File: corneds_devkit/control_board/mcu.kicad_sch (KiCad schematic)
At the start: 1 part, among them U1 nRF52832-QFxx

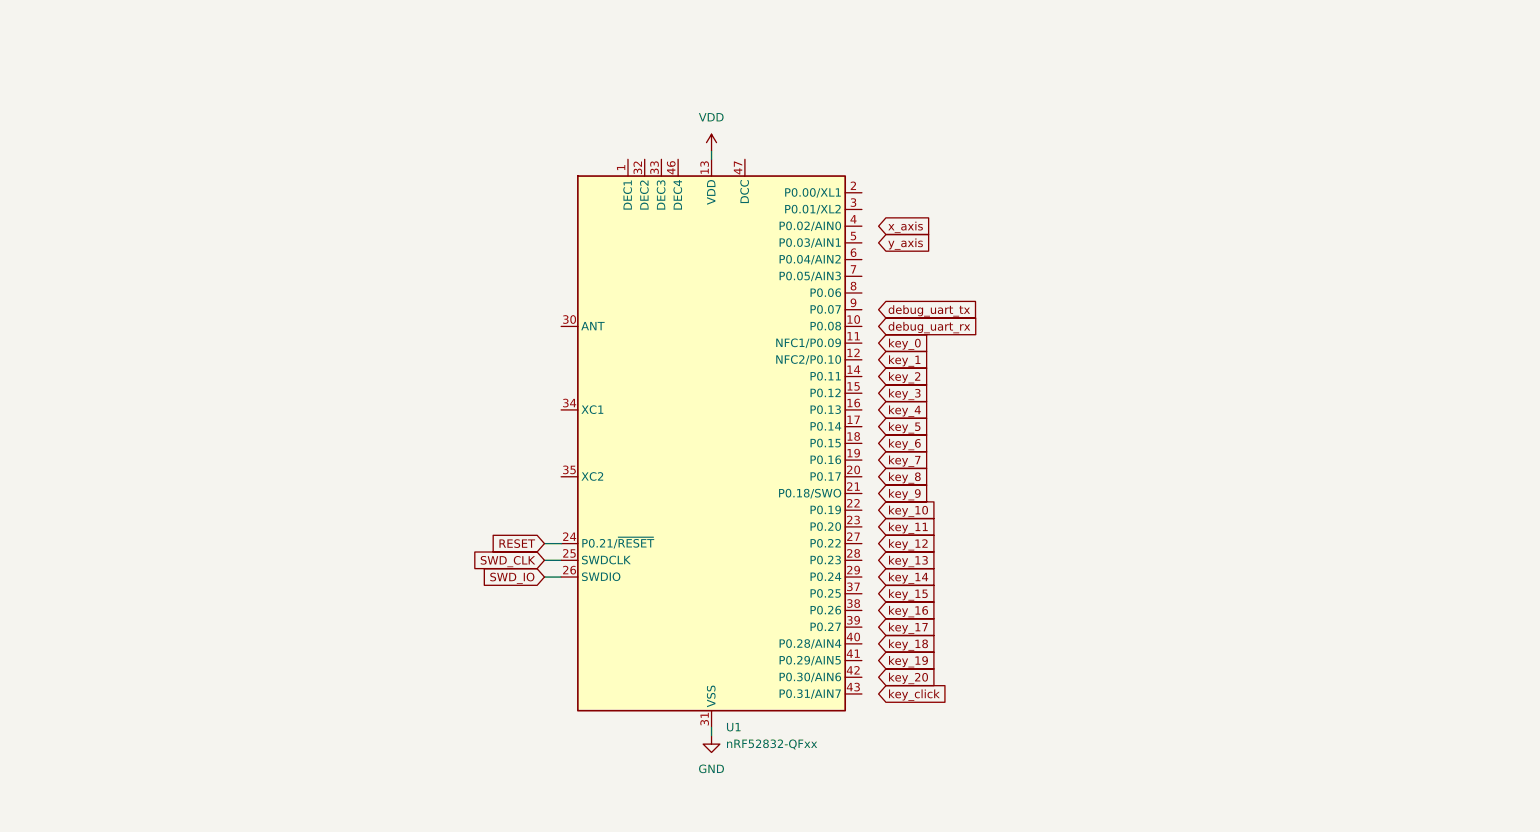
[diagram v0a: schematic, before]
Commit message: finished routing power board and started on control board schematic but realized I need seperate reset lines
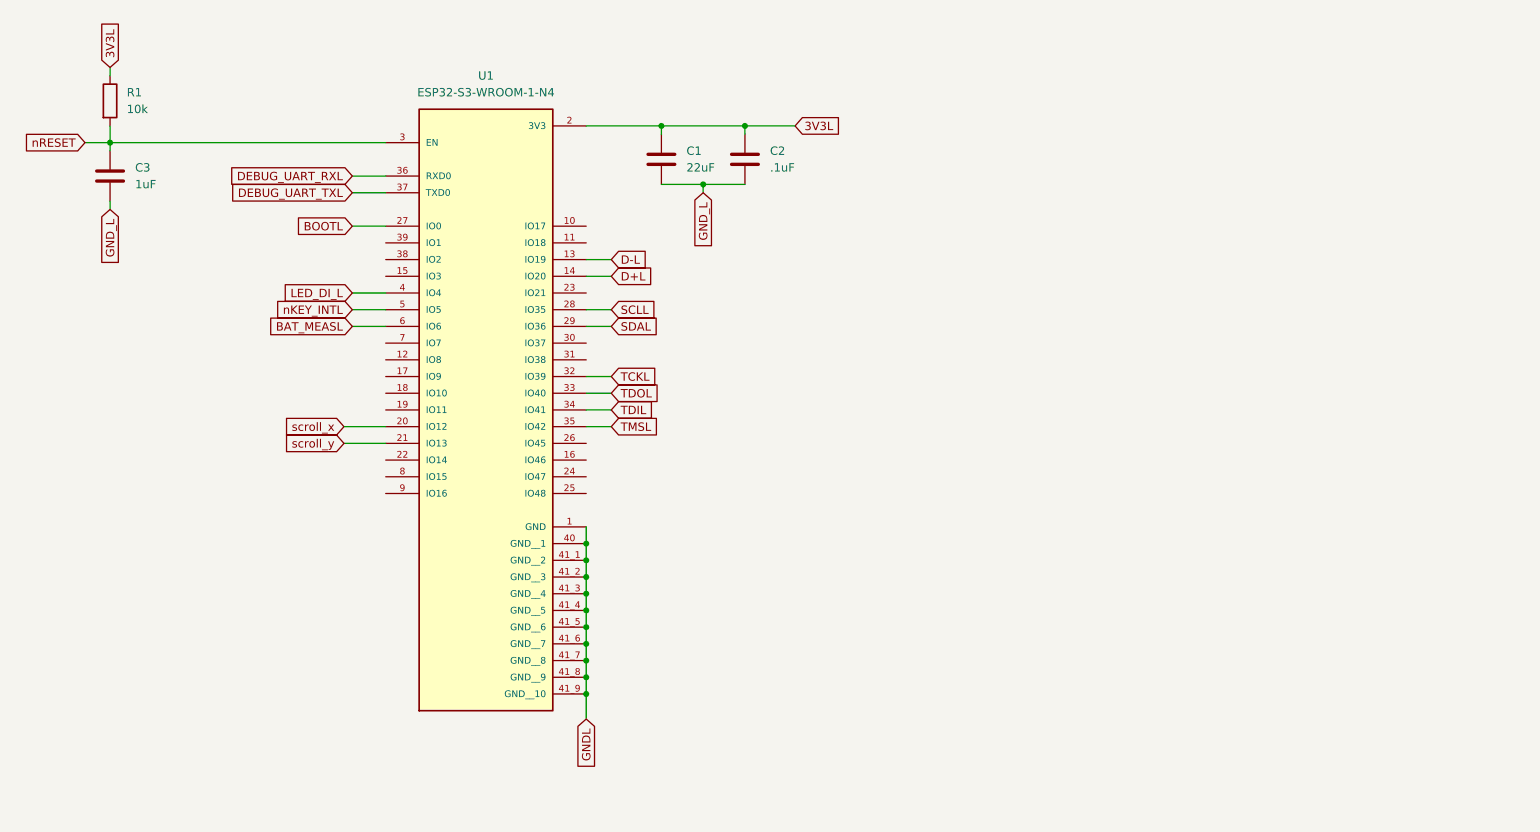
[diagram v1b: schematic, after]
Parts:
- removed U1: nRF52832-QFxx, Package_DFN_QFN:QFN-48-1EP_6x6mm_P0.4mm_EP4.6x4.6mm, symbol MCU_Nordic:nRF52832-QFxx
- added C1: 22uF, Capacitor_SMD:C_0402_1005Metric, symbol Device:C
- added C2: .1uF, Capacitor_SMD:C_0402_1005Metric, symbol Device:C
- added C3: 1uF, Capacitor_SMD:C_0402_1005Metric, symbol Device:C
- added R1: 10k, Resistor_SMD:R_0402_1005Metric, symbol Device:R
- added U1: ESP32-S3-WROOM-1-N4, ESP32-S3-WROOM-1-N4:XCVR_ESP32-S3-WROOM-1-N4, symbol ESP32-S3-WROOM-1-N4:ESP32-S3-WROOM-1-N4
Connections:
- new net 3V3L: C1.1, C2.1, R1.1, U1.2 (3V3)
- new net BAT_MEASL: U1.6 (IO6)
- new net BOOTL: U1.27 (IO0)
- new net D+L: U1.14 (IO20)
- new net D-L: U1.13 (IO19)
- new net DEBUG_UART_RXL: U1.36 (RXD0)
- new net DEBUG_UART_TXL: U1.37 (TXD0)
- new net GNDL: U1.1 (GND), U1.40 (GND__1), U1.41_1 (GND__2), U1.41_2 (GND__3), U1.41_3 (GND__4), U1.41_4 (GND__5), U1.41_5 (GND__6), U1.41_6 (GND__7), U1.41_7 (GND__8), U1.41_8 (GND__9), U1.41_9 (GND__10)
- new net GND_L: C1.2, C2.2, C3.2
- new net LED_DI_L: U1.4 (IO4)
- new net SCLL: U1.28 (IO35)
- new net SDAL: U1.29 (IO36)
- new net TCKL: U1.32 (IO39)
- new net TDIL: U1.34 (IO41)
- new net TDOL: U1.33 (IO40)
- new net TMSL: U1.35 (IO42)
- new net nKEY_INTL: U1.5 (IO5)
- new net nRESET: C3.1, R1.2, U1.3 (EN)
- new net scroll_x: U1.20 (IO12)
- new net scroll_y: U1.21 (IO13)

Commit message: ordered devkit rev A
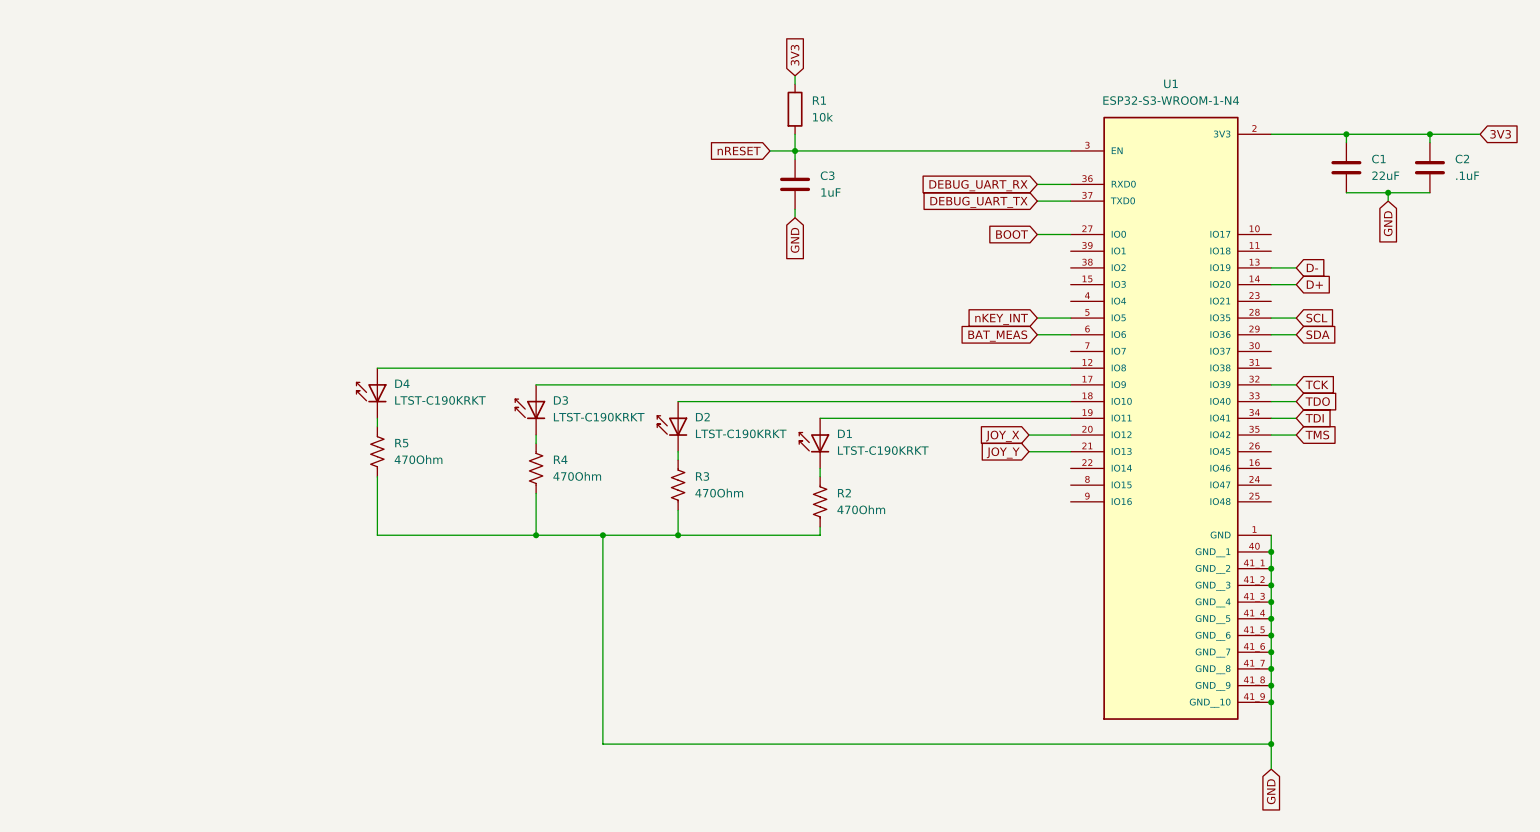
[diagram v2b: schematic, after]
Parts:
- added D1, D2, D3, D4: LTST-C190KRKT, LED_SMD:LED_0603_1608Metric, symbol LED:CQY99
- added R2, R3, R4, R5: 470Ohm, Resistor_SMD:R_0402_1005Metric, symbol Device:R_US
- C1: footprint Capacitor_SMD:C_0402_1005Metric -> Capacitor_SMD:C_0603_1608Metric
- U1: footprint ESP32-S3-WROOM-1-N4:XCVR_ESP32-S3-WROOM-1-N4 -> entropy:XCVR_ESP32-S3-WROOM-1-N4
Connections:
- net GND_L is gone; now on net GND: C1.2, C2.2, C3.2
- net at U1.12 (IO8): now also D4.2 (A)
- net at U1.17 (IO9): now also D3.2 (A)
- net at U1.18 (IO10): now also D2.2 (A)
- net at U1.19 (IO11): now also D1.2 (A)
- net 3V3L renamed 3V3
- net BAT_MEASL renamed BAT_MEAS
- net BOOTL renamed BOOT
- net D+L renamed D+
- net D-L renamed D-
- net DEBUG_UART_RXL renamed DEBUG_UART_RX
- net DEBUG_UART_TXL renamed DEBUG_UART_TX
- net GNDL renamed GND
- net GND: now also R2.1, R3.1, R4.1, R5.1
- net LED_DI_L: no longer names the net of U1.4 (IO4)
- net SCLL renamed SCL
- net SDAL renamed SDA
- net TCKL renamed TCK
- net TDIL renamed TDI
- net TDOL renamed TDO
- net TMSL renamed TMS
- net nKEY_INTL renamed nKEY_INT
- net scroll_x renamed JOY_X
- net scroll_y renamed JOY_Y
- new net: D1.1 (K), R2.2
- new net: D2.1 (K), R3.2
- new net: D3.1 (K), R4.2
- new net: D4.1 (K), R5.2
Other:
- moved on the sheet: C1, C2, C3, R1, U1
